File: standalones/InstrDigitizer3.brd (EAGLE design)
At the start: 28.2 x 76.2 mm, 78 parts, among them Q1 310mA/60V/1.6Ω, U1 LTC2251, U2 MCP4725, U3 LT5560, U4 MCP1703CB, U5 MCP4725

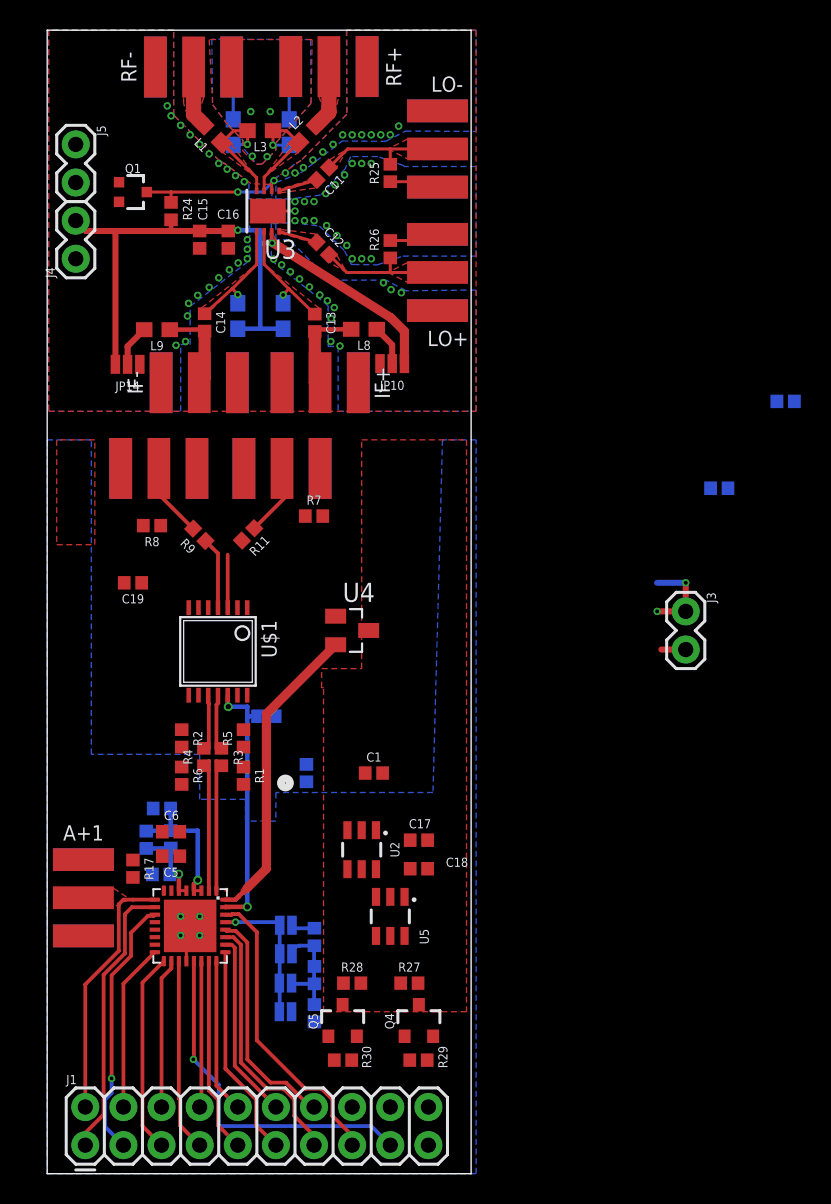
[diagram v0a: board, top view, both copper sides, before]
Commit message: New board in Standalones, InstrDigitizer(4/5)
added new parts with old ADC and capability to break away individual ICs.
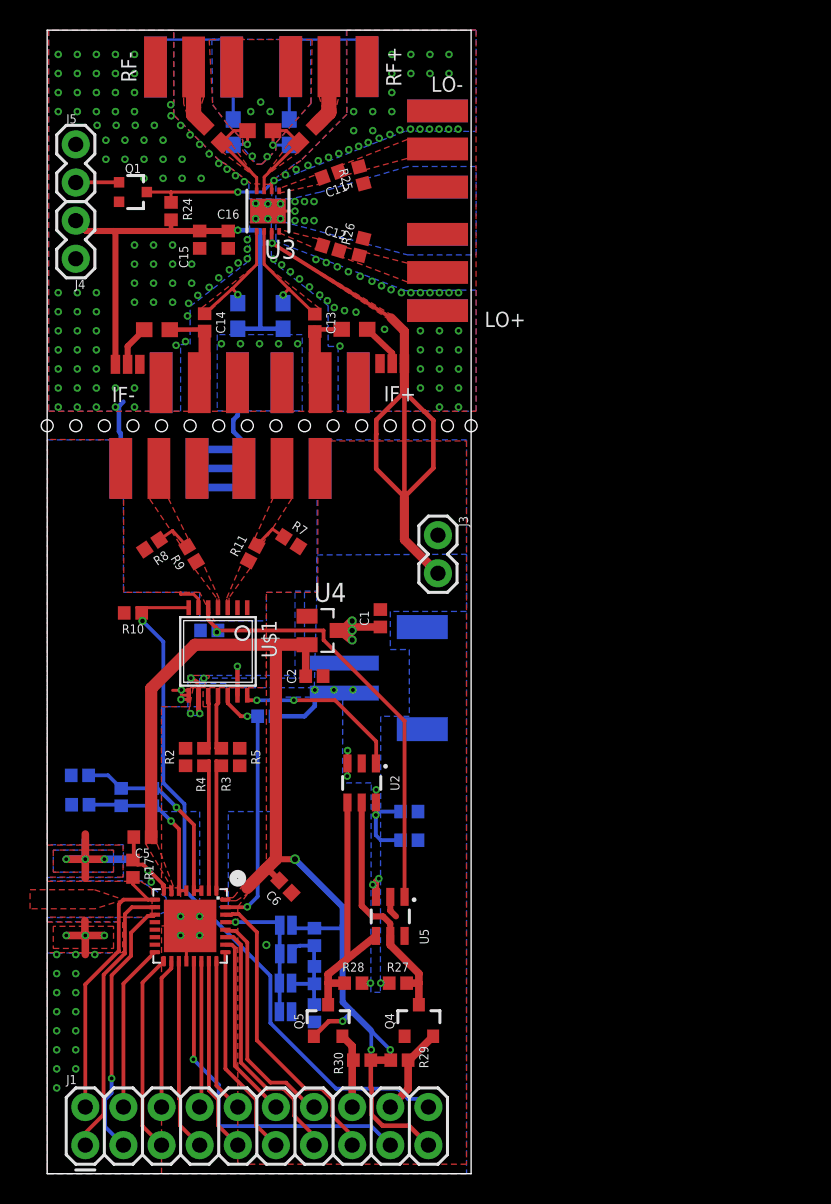
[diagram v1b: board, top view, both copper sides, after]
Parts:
- removed A+1: LINX-SMA-EDGE-0.062, connector:CONSMA003.062
- removed R1, R21, R22, R6: (no value), SparkFun-Resistors:0402
- added J2: (no value), SparkFun-Connectors:JST-2-SMD
- added R10: (no value), SparkFun-Resistors:0402
- R2, R5: value (none) -> 0
- moved J3 17.3 mm to (26.0, 50.2)
- moved C1 10.3 mm to (22.2, 44.6), turned to 90 degrees
- moved C6 8.45 mm to (15.9, 26.7), turned to 315 degrees
- moved C9 7.11 mm to (2.21, 32.2)
- moved C2 6.47 mm to (17.8, 40.8), flipped to the top, turned to 0 degrees
- moved C19 5.99 mm to (10.8, 43.8), flipped to the bottom, turned to 0 degrees
- moved C10 5.89 mm to (2.18, 34.2)
- moved U2 4.45 mm to (21.0, 33.7)
- moved C8 4.34 mm to (4.93, 32.7)
- moved C7 2.87 mm to (7.01, 32.7)
- moved C5 2.29 mm to (6.35, 30.0)
- moved R7 2.28 mm to (16.3, 49.7), turned to 327 degrees
- moved C17 2.01 mm to (24.1, 31.8), flipped to the bottom, turned to 180 degrees
- moved C18 2.01 mm to (24.1, 29.8), flipped to the bottom, turned to 180 degrees
- moved R25 1.94 mm to (20.9, 74.1), turned to 105 degrees
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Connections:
- removed net N$8: J1.20
- removed net N$9: J1.19
- new net N$3: J5.2, Q1.1
- net 3.3V: now also J1.19
- net A_PDN: now also J1.20, R10.1
- net GND: now also J2.1; no longer A+1.GND3, A+1.GND4, R21.1, R21.2, R22.1, R22.2
- net N$1: no longer R7.1
- net N$10: now also R7.1
- net N$11: no longer R8.1
- net N$2: now also R8.1
- net N$4: no longer R1.1
- net N$5: no longer R5.1
- net N$6: no longer R2.1
- net N$7: no longer R6.1
- net SMP_CLK: no longer A+1.ANT
- net VCCA: now also J2.2
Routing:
- net GND: track 23.1 -> 81.4 mm, vias 78 -> 229
- net 3.3V: track 22.0 -> 78.1 mm, vias 0 -> 4
- net VCCA: track 47.9 -> 98.8 mm, vias 2 -> 17
- net A_PDN: track 0.00 -> 47.7 mm, vias 0 -> 1
- net VGC: track 0.00 -> 29.1 mm, vias 0 -> 1
- net SDA_5V: track 0.00 -> 18.1 mm
- net SCL_5V: track 0.00 -> 16.3 mm
- net VC_CTRL: track 0.00 -> 11.5 mm, vias 0 -> 2
- net LO-: track 8.77 -> 0.00 mm
- net LO+: track 8.70 -> 0.00 mm
- net N$1: track 8.14 -> 0.00 mm
- net SCL_3V3: track 0.00 -> 5.94 mm
- net N$23: track 5.69 -> 11.3 mm
- net SDA_3V3: track 0.00 -> 4.98 mm
- net N$11: track 4.79 -> 0.00 mm
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- added copper zone on layer 1, net N$1
- added copper zone on layer 1, net N$10
- added copper zone on layer 1, net N$11
- added copper zone on layer 1, net N$2
- added copper zone on layer 16, net VCCA
